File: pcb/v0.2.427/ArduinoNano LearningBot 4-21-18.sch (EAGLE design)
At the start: 21 parts

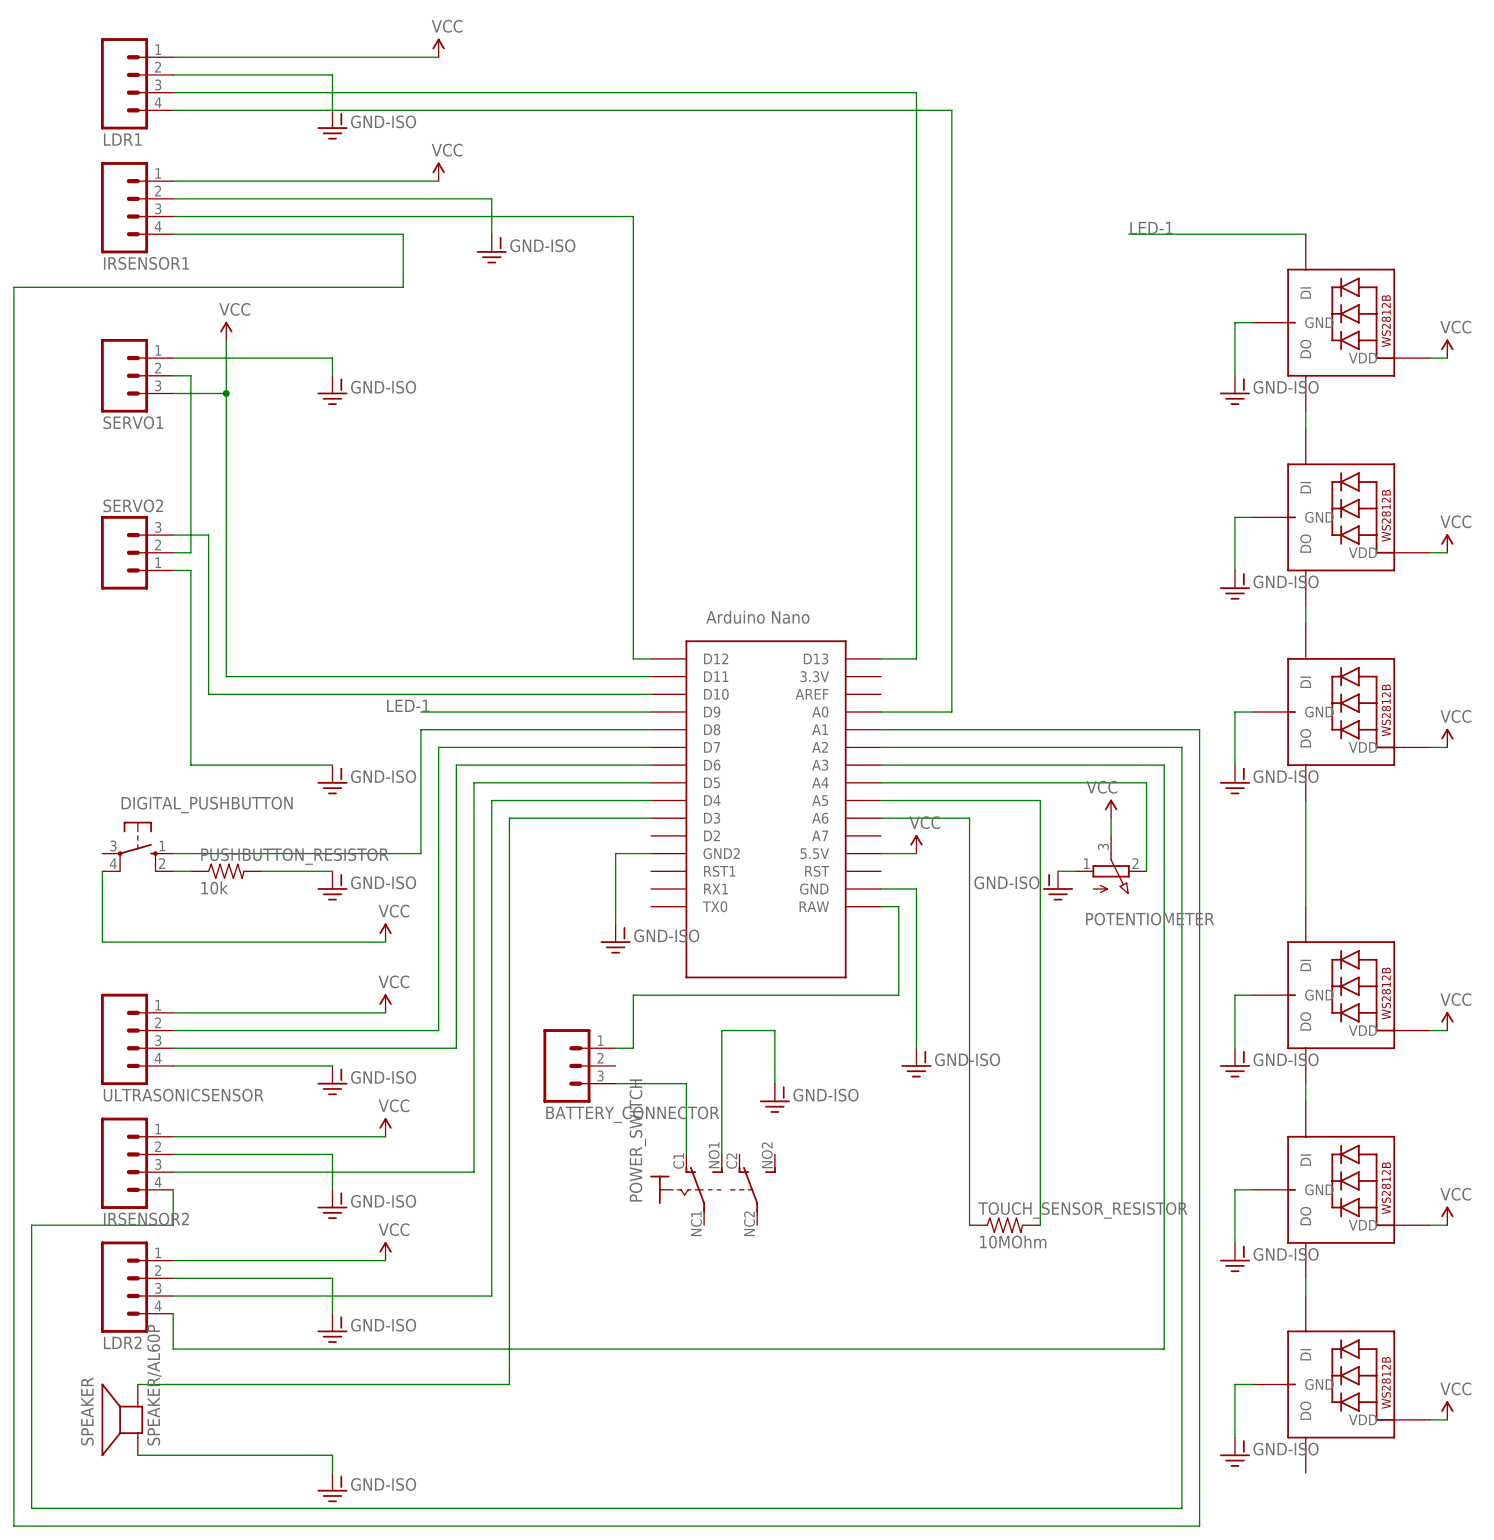
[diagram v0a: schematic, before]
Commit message: changed designators and holes
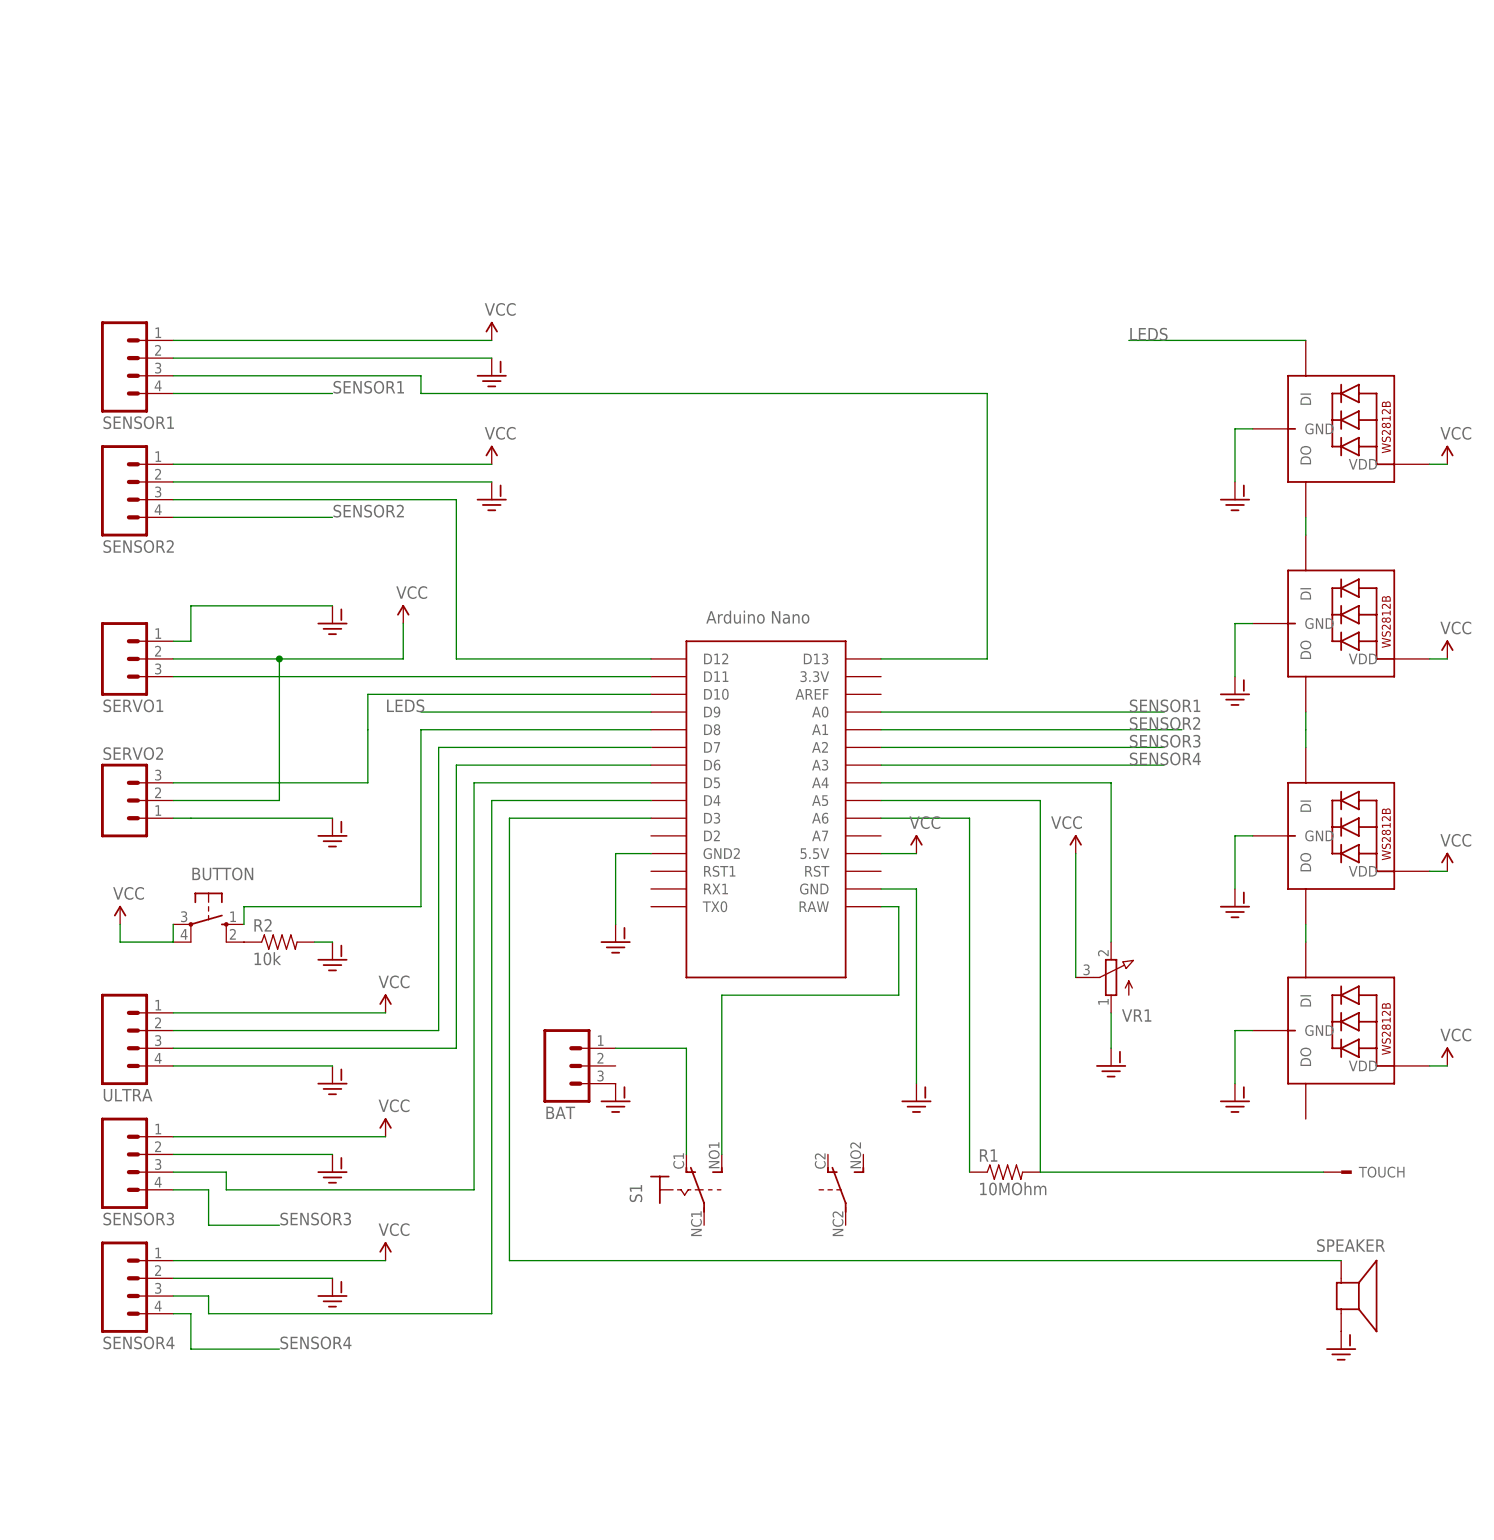
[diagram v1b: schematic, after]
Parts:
- removed BATTERY_CONNECTOR: (no value), SparkFun-Connectors:M03JST-PTH-VERT
- removed DIGITAL_PUSHBUTTON: (no value), switch-omron:10-XX
- removed IRSENSOR1, LDR1: (no value), SparkFun-Connectors:M04LOCK
- removed LED-1, LED-2, LED-3, LED-4, LED-5, LED-6: WS2812B5050, adafruit:WS2812B5050
- removed POTENTIOMETER: (no value), pot:3RP/1610N-VERTICAL
- removed POWER_SWITCH: (no value), ArduinoNano LearningBot 3-15-18:SWITCH_320-938
- removed PUSHBUTTON_RESISTOR: 10k, SparkFun-Passives:RESISTORPTH-1/4W
- removed TOUCH_SENSOR_RESISTOR: 10MOhm, SparkFun-Passives:RESISTORPTH-1/4W
- added BAT: (no value), SparkFun-Connectors:M03POLAR
- added BUTTON: (no value), switch-omron:10-XX
- added LED1, LED2, LED3, LED4: WS2812B5050, adafruit:WS2812B5050
- added R1: 10MOhm, SparkFun-Passives:RESISTORPTH-1/4W
- added R2: 10k, SparkFun-Passives:RESISTORPTH-1/4W
- added S1: (no value), ArduinoNano LearningBot 4-21-18:SWITCH_320-938
- added SENSOR1, SENSOR2: (no value), SparkFun-Connectors:M04LOCK
- added TOUCH: TOUCHSENSOR, CapTouch:TOUCHSENSOR
- added VR1: (no value), pot:3RP/1610N-VERTICAL
- renumbered IRSENSOR2 to SENSOR3, LDR2 to SENSOR4, ULTRASONICSENSOR to ULTRA
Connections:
- net IR_SENSOR2_AO renamed SENSOR3
- net LDR2_AO renamed SENSOR4
- removed net CAP_TOUCH_SEND_PIN: TOUCH_SENSOR_RESISTOR.2, U$1.A5
- removed net IR_SENSOR1_AO: IRSENSOR1.4, U$1.A1
- removed net LDR1_AO: LDR1.4, U$1.A0
- removed net LED-1: LED-2.DI, U$1.D9
- removed net SERVOVCC: SERVO1.2, SERVO2.2
- new net GND-ISO: BAT.3
- new net LEDS: LED1.DI, U$1.D9
- new net SENSOR1: SENSOR1.4, U$1.A0
- new net SENSOR2: SENSOR2.4, U$1.A1
- new net TOUCH: R1.2, TOUCH.1, U$1.A5
- net BUTTON: now also BUTTON.S; no longer DIGITAL_PUSHBUTTON.S
- net CAP_TOUCH_RECEIVE_PIN: now also R1.1; no longer TOUCH_SENSOR_RESISTOR.1
- net GND: now also LED1.GND, LED2.GND, LED3.GND, LED4.GND, R2.2, SENSOR1.2, SENSOR2.2, VR1.A; no longer IRSENSOR1.2, LDR1.2, LED-1.GND, LED-2.GND, LED-3.GND, LED-4.GND, LED-5.GND, LED-6.GND, POTENTIOMETER.A, POWER_SWITCH1.S, PUSHBUTTON_RESISTOR.2
- net IR_SENSOR1_DO: now also SENSOR2.3; no longer IRSENSOR1.3
- net LDR1_DO: now also SENSOR1.3; no longer LDR1.3
- net N$1: now also LED2.DO; no longer LED-1.DI, LED-3.DO
- net N$2: now also LED3.DI; no longer LED-4.DO, LED-5.DI
- net N$3: now also BUTTON.S1, R2.1; no longer DIGITAL_PUSHBUTTON.S1, PUSHBUTTON_RESISTOR.1
- net N$4: now also LED3.DO, LED4.DI; no longer LED-5.DO, LED-6.DI
- net N$5: now also LED1.DO, LED2.DI; no longer LED-2.DO, LED-3.DI
- net N$6: now also SERVO1.3, U$1.D11; no longer LED-1.DO, LED-4.DI
- net N$9: now also BAT.1, S11.O; no longer BATTERY_CONNECTOR.3, POWER_SWITCH1.O
- net POTPIN: now also VR1.E; no longer POTENTIOMETER.E
- net RAWIN: now also S11.S; no longer BATTERY_CONNECTOR.1
- net VCC: now also BUTTON.P, BUTTON.P1, LED1.VDD, LED2.VDD, LED3.VDD, LED4.VDD, SENSOR1.1, SENSOR2.1, SERVO1.2, SERVO2.2, VR1.S; no longer DIGITAL_PUSHBUTTON.P1, IRSENSOR1.1, LDR1.1, LED-1.VDD, LED-2.VDD, LED-3.VDD, LED-4.VDD, LED-5.VDD, LED-6.VDD, POTENTIOMETER.S, SERVO1.3, U$1.D11
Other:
- moved on the sheet: SERVO1, SERVO2, SPEAKER

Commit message: most recent board
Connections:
- removed net GND-ISO: BAT.3
- removed net N$2: LED3.DI
- net GND: now also BAT.3
- net N$1: now also LED3.DI
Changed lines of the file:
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@@
 <?xml version="1.0" encoding="utf-8"?>
 <!DOCTYPE eagle SYSTEM "eagle.dtd">
-<eagle version="8.4.0">
+<eagle version="8.4.1">
 <drawing>
 <settings>
@@
 <part name="GND15" library="SparkFun-Aesthetics" deviceset="GND-ISO" device=""/>
 <part name="TOUCH" library="CapTouch" deviceset="TOUCHSENSOR" device=""/>
-<part name="GND16" library="SparkFun-Aesthetics" deviceset="GND-ISO" device=""/>
+<part name="GND" library="SparkFun-Aesthetics" deviceset="GND-ISO" device=""/>
 </parts>
 <sheets>
@@
 <attribute name="NAME" x="208.28" y="62.738" size="1.524" layer="95"/>
 </instance>
-<instance part="GND16" gate="G$1" x="101.6" y="73.66" smashed="yes">
-<attribute name="VALUE" x="104.14" y="73.66" size="1.778" layer="96" display="off"/>
+<instance part="GND" gate="G$1" x="106.68" y="73.66" smashed="yes">
+<attribute name="VALUE" x="109.22" y="73.66" size="1.778" layer="96" display="off"/>
 </instance>
 </instances>
@@
 </segment>
 </net>
-<net name="N$2" class="0">
-<segment>
-<pinref part="LED3" gate="G$1" pin="DI"/>
-<wire x1="200.66" y1="127" x2="200.66" y2="124.46" width="0.1524" layer="91"/>
-</segment>
-</net>
 <net name="N$4" class="0">
 <segment>
@@
 </segment>
 </net>
-<net name="N$1" class="0">
-<segment>
-<pinref part="LED2" gate="G$1" pin="DO"/>
-<wire x1="200.66" y1="129.54" x2="200.66" y2="127" width="0.1524" layer="91"/>
-</segment>
-</net>
 <net name="ECHO_PIN" class="0">
 <segment>
@@
 <wire x1="144.78" y1="104.14" x2="144.78" y2="76.2" width="0.1524" layer="91"/>
 </segment>
+<segment>
+<pinref part="BAT" gate="J$1" pin="3"/>
+<pinref part="GND" gate="G$1" pin="GND-ISO"/>
+<wire x1="106.68" y1="76.2" x2="101.6" y2="76.2" width="0.1524" layer="91"/>
+</segment>
 </net>
 <net name="BUTTON1" class="0">
@@
 </segment>
 </net>
-<net name="GND-ISO" class="0">
-<segment>
-<pinref part="BAT" gate="J$1" pin="3"/>
-<pinref part="GND16" gate="G$1" pin="GND-ISO"/>
-</segment>
-</net>
+<net name="N$1" class="0">
+<segment>
+<pinref part="LED2" gate="G$1" pin="DO"/>
+<pinref part="LED3" gate="G$1" pin="DI"/>
+<wire x1="200.66" y1="129.54" x2="200.66" y2="124.46" width="0.1524" layer="91"/>
+</segment>
+</net>

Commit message: with gerbers
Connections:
- net VCC: no longer BUTTON.P
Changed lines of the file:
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@@
 <wire x1="30.48" y1="96.52" x2="30.48" y2="99.06" width="0.1524" layer="91"/>
 <wire x1="38.1" y1="96.52" x2="30.48" y2="96.52" width="0.1524" layer="91"/>
-<pinref part="BUTTON" gate="1" pin="P"/>
-<wire x1="38.1" y1="99.06" x2="38.1" y2="96.52" width="0.1524" layer="91"/>
 </segment>
 <segment>
@@
 <net name="TOUCH" class="0">
 <segment>
-<pinref part="U$1" gate="G$1" pin="A5"/>
-<wire x1="139.7" y1="116.84" x2="162.56" y2="116.84" width="0.1524" layer="91"/>
-<wire x1="162.56" y1="116.84" x2="162.56" y2="63.5" width="0.1524" layer="91"/>
 <pinref part="R1" gate="G$1" pin="2"/>
 <wire x1="162.56" y1="63.5" x2="203.2" y2="63.5" width="0.1524" layer="91"/>
 <pinref part="TOUCH" gate="G$2" pin="1"/>
-</segment>
-</net>
+<pinref part="U$1" gate="G$1" pin="A5"/>
+<wire x1="139.7" y1="116.84" x2="162.56" y2="116.84" width="0.1524" layer="91"/>
+<wire x1="162.56" y1="63.5" x2="162.56" y2="116.84" width="0.1524" layer="91"/>
+<junction x="162.56" y="63.5"/>
+</segment>
+</net>
